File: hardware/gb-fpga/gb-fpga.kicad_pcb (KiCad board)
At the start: 2 copper layers, 1 part, among them U1 xc7s25ftgb196

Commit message: Basic boards setup
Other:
- copper layers 2 -> 4
- net class Default: via_dia 0.8 -> 0.5; via_drill 0.4 -> 0.3
- rule trace_min: 0.2 -> 0.15
- rule via_min_drill: 0.3 -> 0.2
- rule via_min_size: 0.4 -> 0.35
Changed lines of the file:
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@@
   (layers
     (0 F.Cu signal)
+    (1 In1.Cu power)
+    (2 In2.Cu power)
     (31 B.Cu signal)
     (32 B.Adhes user)
@@
     (zone_clearance 0.508)
     (zone_45_only no)
-    (trace_min 0.2)
-    (via_size 0.8)
-    (via_drill 0.4)
-    (via_min_size 0.4)
-    (via_min_drill 0.3)
+    (trace_min 0.15)
+    (via_size 0.5)
+    (via_drill 0.3)
+    (via_min_size 0.35)
+    (via_min_drill 0.2)
     (uvia_size 0.3)
     (uvia_drill 0.1)
@@
     (pcb_text_size 1.5 1.5)
     (mod_edge_width 0.12)
-    (mod_text_size 1 1)
+    (mod_text_size 1 0.8)
     (mod_text_width 0.15)
     (pad_size 1.524 1.524)
@@
     (clearance 0.2)
     (trace_width 0.25)
-    (via_dia 0.8)
-    (via_drill 0.4)
+    (via_dia 0.5)
+    (via_drill 0.3)
     (uvia_dia 0.3)
     (uvia_drill 0.1)

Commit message: Add GND net
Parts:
- added U2: MX25R3235FZNxx1, Package_SON:WSON-8-1EP_6x5mm_P1.27mm_EP3.4x4mm, F.Cu at (163.9, 30.7)
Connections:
- net Net-(U1-PadA1) renamed GND

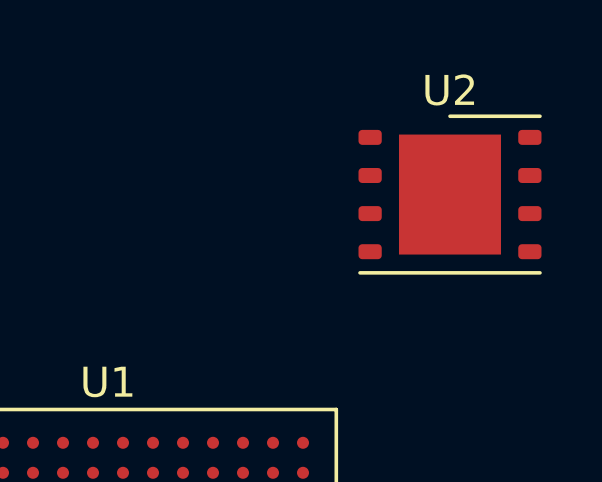
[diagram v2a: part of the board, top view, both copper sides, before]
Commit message: Use USON footprint for flash memory
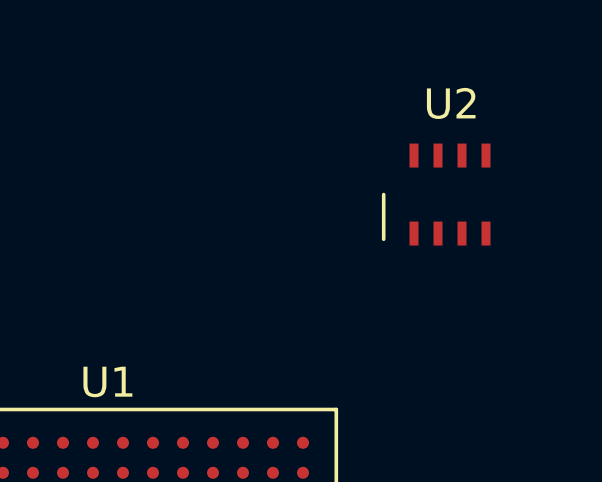
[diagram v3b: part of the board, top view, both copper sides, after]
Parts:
- U2: value MX25R3235FZNxx1 -> MX25R3235FZBxx1; footprint Package_SON:WSON-8-1EP_6x5mm_P1.27mm_EP3.4x4mm -> Package_SON:USON-8_4.0x3.0mm_P0.8mm
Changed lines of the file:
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@@
       (effects (font (size 1 1) (thickness 0.15)))
     )
+    (fp_line (start -7.61 7.61) (end -7.61 -6.61) (layer F.SilkS) (width 0.12))
+    (fp_line (start 7.61 7.61) (end -7.61 7.61) (layer F.SilkS) (width 0.12))
+    (fp_line (start 7.61 -7.61) (end 7.61 7.61) (layer F.SilkS) (width 0.12))
+    (fp_line (start -6.61 -7.61) (end 7.61 -7.61) (layer F.SilkS) (width 0.12))
+    (fp_line (start 8.5 -8.5) (end -8.5 -8.5) (layer F.CrtYd) (width 0.05))
+    (fp_line (start 8.5 8.5) (end 8.5 -8.5) (layer F.CrtYd) (width 0.05))
+    (fp_line (start -8.5 8.5) (end 8.5 8.5) (layer F.CrtYd) (width 0.05))
+    (fp_line (start -8.5 -8.5) (end -8.5 8.5) (layer F.CrtYd) (width 0.05))
+    (fp_line (start 7.5 -7.5) (end 7.5 7.5) (layer F.Fab) (width 0.1))
+    (fp_line (start -6.5 -7.5) (end 7.5 -7.5) (layer F.Fab) (width 0.1))
+    (fp_line (start -7.5 -6.5) (end -6.5 -7.5) (layer F.Fab) (width 0.1))
+    (fp_line (start -7.5 7.5) (end -7.5 -6.5) (layer F.Fab) (width 0.1))
     (fp_line (start 7.5 7.5) (end -7.5 7.5) (layer F.Fab) (width 0.1))
-    (fp_line (start -7.5 7.5) (end -7.5 -6.5) (layer F.Fab) (width 0.1))
-    (fp_line (start -7.5 -6.5) (end -6.5 -7.5) (layer F.Fab) (width 0.1))
-    (fp_line (start -6.5 -7.5) (end 7.5 -7.5) (layer F.Fab) (width 0.1))
-    (fp_line (start 7.5 -7.5) (end 7.5 7.5) (layer F.Fab) (width 0.1))
-    (fp_line (start -8.5 -8.5) (end -8.5 8.5) (layer F.CrtYd) (width 0.05))
-    (fp_line (start -8.5 8.5) (end 8.5 8.5) (layer F.CrtYd) (width 0.05))
-    (fp_line (start 8.5 8.5) (end 8.5 -8.5) (layer F.CrtYd) (width 0.05))
-    (fp_line (start 8.5 -8.5) (end -8.5 -8.5) (layer F.CrtYd) (width 0.05))
-    (fp_line (start -6.61 -7.61) (end 7.61 -7.61) (layer F.SilkS) (width 0.12))
-    (fp_line (start 7.61 -7.61) (end 7.61 7.61) (layer F.SilkS) (width 0.12))
-    (fp_line (start 7.61 7.61) (end -7.61 7.61) (layer F.SilkS) (width 0.12))
-    (fp_line (start -7.61 7.61) (end -7.61 -6.61) (layer F.SilkS) (width 0.12))
     (fp_text user %R (at 0 0) (layer F.Fab)
       (effects (font (size 1 1) (thickness 0.15)))
@@
     )
   )
-  (module Package_SON:WSON-8-1EP_6x5mm_P1.27mm_EP3.4x4mm (layer F.Cu)
+  (module Package_SON:USON-8_4.0x3.0mm_P0.8mm (layer F.Cu)
     (at 163.9 30.725)
-    (descr "WSON, 8 Pin (http://ww1.microchip.com/downloads/en/AppNotes/S72030.pdf), generated with kicad-footprint-generator ipc_noLead_generator.py")
-    (tags "WSON NoLead")
-    (attr smd)
-    (fp_text reference U2 (at 0 -3.45) (layer F.SilkS)
+    (fp_text reference U2 (at 0.05 -3) (layer F.SilkS)
       (effects (font (size 1 1) (thickness 0.15)))
     )
-    (fp_text value MX25R3235FZNxx1 (at 0 3.45) (layer F.Fab)
+    (fp_text value MX25R3235FZBxx1 (at -0.06 3.13) (layer F.Fab)
       (effects (font (size 1 1) (thickness 0.15)))
     )
-    (fp_line (start 3.3 -2.75) (end -3.3 -2.75) (layer F.CrtYd) (width 0.05))
-    (fp_line (start 3.3 2.75) (end 3.3 -2.75) (layer F.CrtYd) (width 0.05))
-    (fp_line (start -3.3 2.75) (end 3.3 2.75) (layer F.CrtYd) (width 0.05))
-    (fp_line (start -3.3 -2.75) (end -3.3 2.75) (layer F.CrtYd) (width 0.05))
-    (fp_line (start -3 -1.5) (end -2 -2.5) (layer F.Fab) (width 0.1))
-    (fp_line (start -3 2.5) (end -3 -1.5) (layer F.Fab) (width 0.1))
-    (fp_line (start 3 2.5) (end -3 2.5) (layer F.Fab) (width 0.1))
-    (fp_line (start 3 -2.5) (end 3 2.5) (layer F.Fab) (width 0.1))
-    (fp_line (start -2 -2.5) (end 3 -2.5) (layer F.Fab) (width 0.1))
-    (fp_line (start -3 2.61) (end 3 2.61) (layer F.SilkS) (width 0.12))
-    (fp_line (start 0 -2.61) (end 3 -2.61) (layer F.SilkS) (width 0.12))
-    (fp_text user %R (at 0 0) (layer F.Fab)
-      (effects (font (size 1 1) (thickness 0.15)))
-    )
-    (pad 1 smd roundrect (at -2.6625 -1.905) (size 0.775 0.5) (layers F.Cu F.Paste F.Mask) (roundrect_rratio 0.25)
+    (fp_line (start 2.39 1.98) (end 2.39 -1.99) (layer F.CrtYd) (width 0.12))
+    (fp_line (start -2.37 1.98) (end 2.39 1.98) (layer F.CrtYd) (width 0.12))
+    (fp_line (start -2.37 -1.99) (end -2.37 1.98) (layer F.CrtYd) (width 0.12))
+    (fp_line (start 2.39 -1.99) (end -2.37 -1.99) (layer F.CrtYd) (width 0.12))
+    (fp_line (start -2 -1.5) (end 2 -1.5) (layer F.Fab) (width 0.12))
+    (fp_line (start 2 -1.5) (end 2 1.5) (layer F.Fab) (width 0.12))
+    (fp_line (start 2 1.5) (end -2 1.5) (layer F.Fab) (width 0.12))
+    (fp_line (start -2 1.5) (end -2 -1.5) (layer F.Fab) (width 0.12))
+    (fp_line (start -2.21 1.49) (end -2.21 0) (layer F.SilkS) (width 0.12))
+    (pad 1 smd rect (at -1.2 1.3) (size 0.3 0.8) (layers F.Cu F.Paste F.Mask)
       (net 129 "Net-(U2-Pad1)"))
-    (pad 2 smd roundrect (at -2.6625 -0.635) (size 0.775 0.5) (layers F.Cu F.Paste F.Mask) (roundrect_rratio 0.25)
+    (pad 2 smd rect (at -0.4 1.3) (size 0.3 0.8) (layers F.Cu F.Paste F.Mask)
       (net 130 "Net-(U2-Pad2)"))
-    (pad 3 smd roundrect (at -2.6625 0.635) (size 0.775 0.5) (layers F.Cu F.Paste F.Mask) (roundrect_rratio 0.25)
+    (pad 3 smd rect (at 0.4 1.3) (size 0.3 0.8) (layers F.Cu F.Paste F.Mask)
       (net 131 "Net-(U2-Pad3)"))
-    (pad 4 smd roundrect (at -2.6625 1.905) (size 0.775 0.5) (layers F.Cu F.Paste F.Mask) (roundrect_rratio 0.25)
-      (net 128 GND))
-    (pad 5 smd roundrect (at 2.6625 1.905) (size 0.775 0.5) (layers F.Cu F.Paste F.Mask) (roundrect_rratio 0.25)
+    (pad 4 smd rect (at 1.2 1.3) (size 0.3 0.8) (layers F.Cu F.Paste F.Mask)
+      (net 128 GND))
+    (pad 5 smd rect (at 1.2 -1.3) (size 0.3 0.8) (layers F.Cu F.Paste F.Mask)
       (net 132 "Net-(U2-Pad5)"))
-    (pad 6 smd roundrect (at 2.6625 0.635) (size 0.775 0.5) (layers F.Cu F.Paste F.Mask) (roundrect_rratio 0.25)
+    (pad 6 smd rect (at 0.4 -1.3) (size 0.3 0.8) (layers F.Cu F.Paste F.Mask)
       (net 6 "Net-(U1-PadA8)"))
-    (pad 7 smd roundrect (at 2.6625 -0.635) (size 0.775 0.5) (layers F.Cu F.Paste F.Mask) (roundrect_rratio 0.25)
+    (pad 7 smd rect (at -0.4 -1.3) (size 0.3 0.8) (layers F.Cu F.Paste F.Mask)
       (net 133 "Net-(U2-Pad7)"))
-    (pad 8 smd roundrect (at 2.6625 -1.905) (size 0.775 0.5) (layers F.Cu F.Paste F.Mask) (roundrect_rratio 0.25)
+    (pad 8 smd rect (at -1.2 -1.3) (size 0.3 0.8) (layers F.Cu F.Paste F.Mask)
       (net 134 "Net-(U2-Pad8)"))
-    (pad 9 smd rect (at 0 0) (size 3.4 4) (layers F.Cu F.Mask)
-      (net 128 GND))
-    (pad "" smd roundrect (at -0.85 -1) (size 1.37 1.61) (layers F.Paste) (roundrect_rratio 0.182482))
-    (pad "" smd roundrect (at -0.85 1) (size 1.37 1.61) (layers F.Paste) (roundrect_rratio 0.182482))
-    (pad "" smd roundrect (at 0.85 -1) (size 1.37 1.61) (layers F.Paste) (roundrect_rratio 0.182482))
-    (pad "" smd roundrect (at 0.85 1) (size 1.37 1.61) (layers F.Paste) (roundrect_rratio 0.182482))
-    (model ${KISYS3DMOD}/Package_SON.3dshapes/WSON-8-1EP_6x5mm_P1.27mm_EP3.4x4mm.wrl
-      (at (xyz 0 0 0))
-      (scale (xyz 1 1 1))
-      (rotate (xyz 0 0 0))
-    )
   )
 )

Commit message: Use human readable names on pcb
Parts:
- U1: value xc7s25ftgb196 -> FPGA
- U2: value MX25R3235FZBxx1 -> Flash
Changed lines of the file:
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@@
       (effects (font (size 1 1) (thickness 0.15)))
     )
-    (fp_text value xc7s25ftgb196 (at 0 8.5) (layer F.Fab)
+    (fp_text value FPGA (at 0 8.5) (layer F.Fab)
       (effects (font (size 1 1) (thickness 0.15)))
     )
@@
       (effects (font (size 1 1) (thickness 0.15)))
     )
-    (fp_text value MX25R3235FZBxx1 (at -0.06 3.13) (layer F.Fab)
+    (fp_text value Flash (at -0.06 3.13) (layer F.Fab)
       (effects (font (size 1 1) (thickness 0.15)))
     )

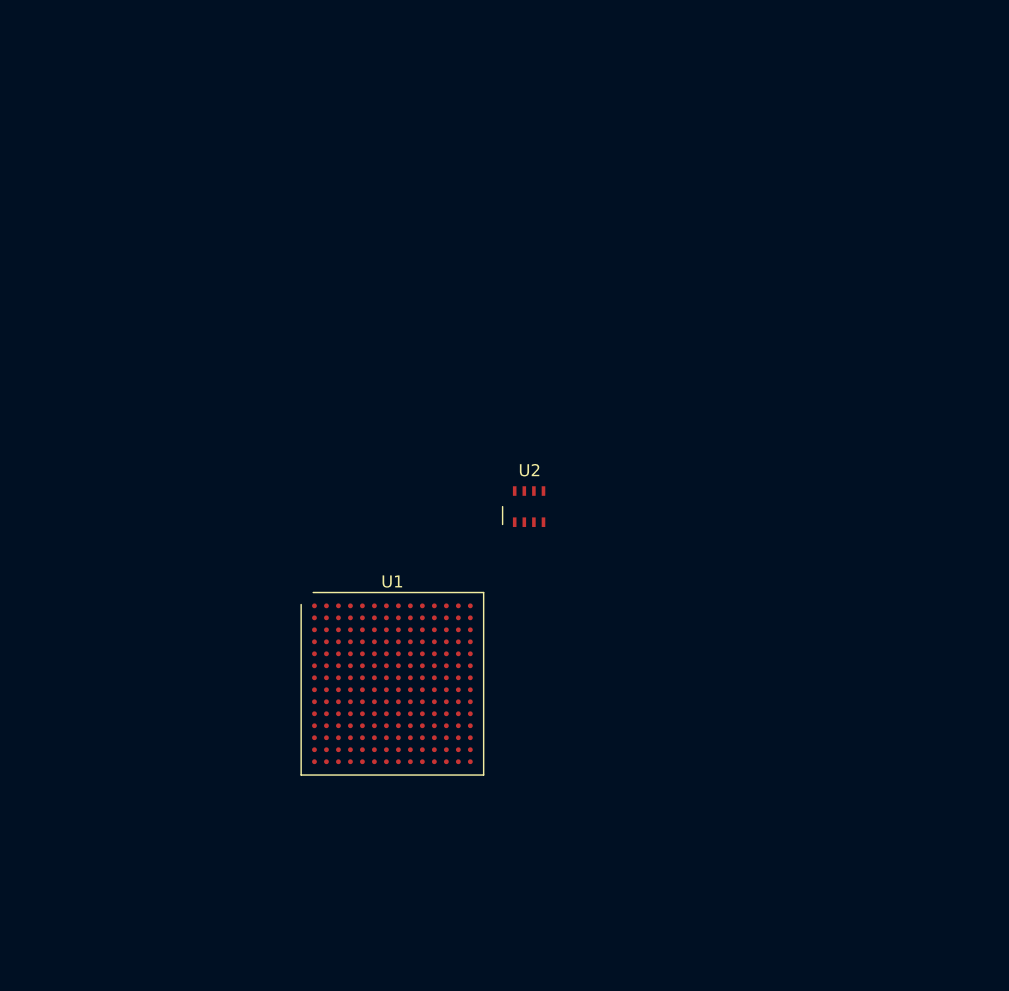
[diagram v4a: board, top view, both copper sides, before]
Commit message: Add board outline
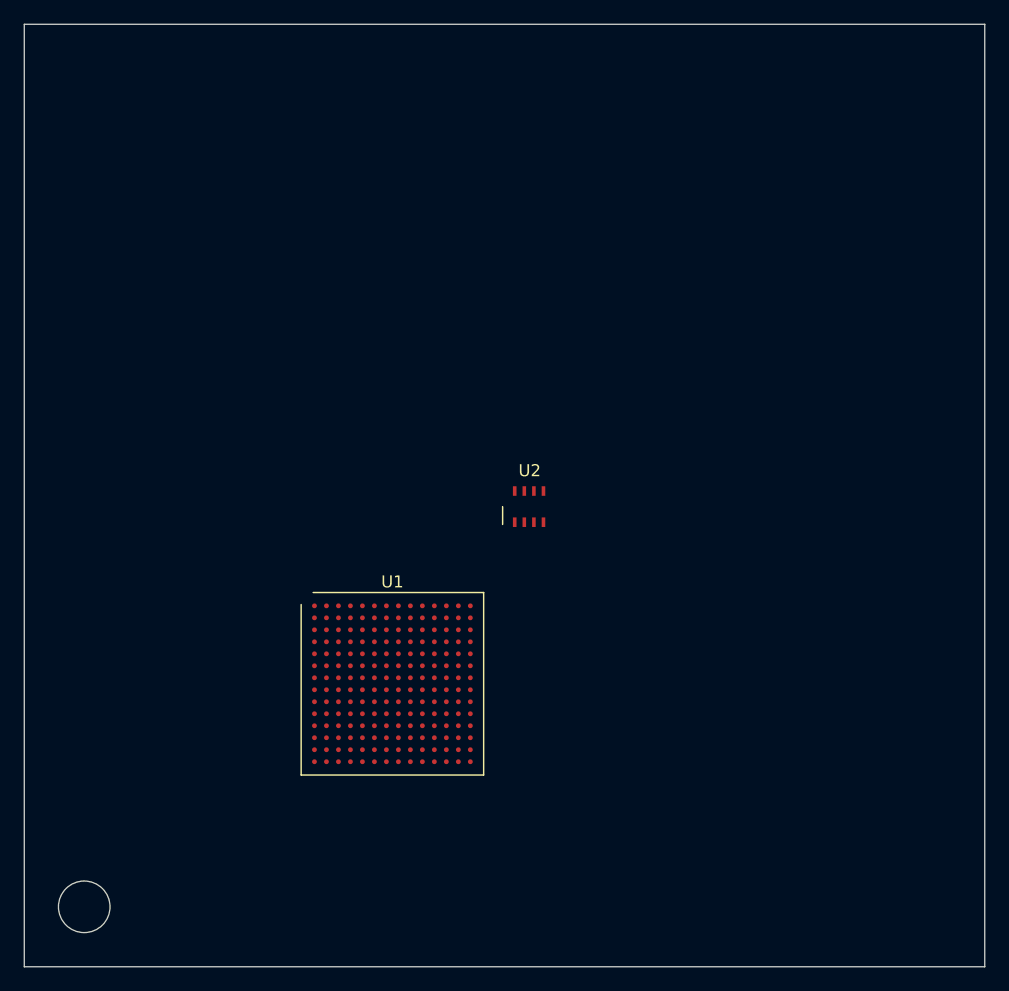
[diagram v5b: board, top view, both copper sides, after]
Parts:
- added REF**: MountingHole_4.3mm_M4_DIN965, MountingHole:MountingHole_4.3mm_M4_DIN965, F.Cu at (126.8, 64.1)
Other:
- board outline added: 80.1 x 78.6 mm
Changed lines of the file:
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@@
   (general
     (thickness 1.6)
-    (drawings 0)
+    (drawings 4)
     (tracks 0)
     (zones 0)
-    (modules 2)
+    (modules 3)
     (nets 135)
   )
@@
     (pad_drill 0.762)
     (pad_to_mask_clearance 0)
-    (aux_axis_origin 0 0)
+    (aux_axis_origin 121.8 69.1)
     (visible_elements FEFFFF7F)
     (pcbplotparams
@@
     (add_net "Net-(U2-Pad8)")
   )
+  (module MountingHole:MountingHole_4.3mm_M4_DIN965 (layer F.Cu)
+    (at 126.8 64.1)
+    (descr "Mounting Hole 4.3mm, no annular, M4, DIN965")
+    (tags "mounting hole 4.3mm no annular m4 din965")
+    (attr virtual)
+    (fp_text reference REF** (at 0 -4.75) (layer F.SilkS) hide
+      (effects (font (size 1 1) (thickness 0.15)))
+    )
+    (fp_text value MountingHole_4.3mm_M4_DIN965 (at 0 4.75) (layer F.Fab) hide
+      (effects (font (size 1 1) (thickness 0.15)))
+    )
+    (fp_text user %R (at 0.3 0) (layer F.Fab) hide
+      (effects (font (size 1 1) (thickness 0.15)))
+    )
+    (fp_circle (center 0 0) (end 3.75 0) (layer Cmts.User) (width 0.15))
+    (fp_circle (center 0 0) (end 4 0) (layer F.CrtYd) (width 0.05))
+    (pad 1 np_thru_hole circle (at 0 0) (size 4.3 4.3) (drill 4.3) (layers *.Cu *.Mask))
+  )
   (module Package_BGA:Xilinx_FTGB196 (layer F.Cu)
     (at 152.5 45.5)
@@
       (effects (font (size 1 1) (thickness 0.15)))
     )
+    (fp_line (start 7.5 7.5) (end -7.5 7.5) (layer F.Fab) (width 0.1))
+    (fp_line (start -7.5 7.5) (end -7.5 -6.5) (layer F.Fab) (width 0.1))
+    (fp_line (start -7.5 -6.5) (end -6.5 -7.5) (layer F.Fab) (width 0.1))
+    (fp_line (start -6.5 -7.5) (end 7.5 -7.5) (layer F.Fab) (width 0.1))
+    (fp_line (start 7.5 -7.5) (end 7.5 7.5) (layer F.Fab) (width 0.1))
+    (fp_line (start -8.5 -8.5) (end -8.5 8.5) (layer F.CrtYd) (width 0.05))
+    (fp_line (start -8.5 8.5) (end 8.5 8.5) (layer F.CrtYd) (width 0.05))
+    (fp_line (start 8.5 8.5) (end 8.5 -8.5) (layer F.CrtYd) (width 0.05))
+    (fp_line (start 8.5 -8.5) (end -8.5 -8.5) (layer F.CrtYd) (width 0.05))
+    (fp_line (start -6.61 -7.61) (end 7.61 -7.61) (layer F.SilkS) (width 0.12))
+    (fp_line (start 7.61 -7.61) (end 7.61 7.61) (layer F.SilkS) (width 0.12))
+    (fp_line (start 7.61 7.61) (end -7.61 7.61) (layer F.SilkS) (width 0.12))
     (fp_line (start -7.61 7.61) (end -7.61 -6.61) (layer F.SilkS) (width 0.12))
-    (fp_line (start 7.61 7.61) (end -7.61 7.61) (layer F.SilkS) (width 0.12))
-    (fp_line (start 7.61 -7.61) (end 7.61 7.61) (layer F.SilkS) (width 0.12))
-    (fp_line (start -6.61 -7.61) (end 7.61 -7.61) (layer F.SilkS) (width 0.12))
-    (fp_line (start 8.5 -8.5) (end -8.5 -8.5) (layer F.CrtYd) (width 0.05))
-    (fp_line (start 8.5 8.5) (end 8.5 -8.5) (layer F.CrtYd) (width 0.05))
-    (fp_line (start -8.5 8.5) (end 8.5 8.5) (layer F.CrtYd) (width 0.05))
-    (fp_line (start -8.5 -8.5) (end -8.5 8.5) (layer F.CrtYd) (width 0.05))
-    (fp_line (start 7.5 -7.5) (end 7.5 7.5) (layer F.Fab) (width 0.1))
-    (fp_line (start -6.5 -7.5) (end 7.5 -7.5) (layer F.Fab) (width 0.1))
-    (fp_line (start -7.5 -6.5) (end -6.5 -7.5) (layer F.Fab) (width 0.1))
-    (fp_line (start -7.5 7.5) (end -7.5 -6.5) (layer F.Fab) (width 0.1))
-    (fp_line (start 7.5 7.5) (end -7.5 7.5) (layer F.Fab) (width 0.1))
     (fp_text user %R (at 0 0) (layer F.Fab)
       (effects (font (size 1 1) (thickness 0.15)))
@@
       (effects (font (size 1 1) (thickness 0.15)))
     )
+    (fp_line (start -2.21 1.49) (end -2.21 0) (layer F.SilkS) (width 0.12))
+    (fp_line (start -2 1.5) (end -2 -1.5) (layer F.Fab) (width 0.12))
+    (fp_line (start 2 1.5) (end -2 1.5) (layer F.Fab) (width 0.12))
+    (fp_line (start 2 -1.5) (end 2 1.5) (layer F.Fab) (width 0.12))
+    (fp_line (start -2 -1.5) (end 2 -1.5) (layer F.Fab) (width 0.12))
+    (fp_line (start 2.39 -1.99) (end -2.37 -1.99) (layer F.CrtYd) (width 0.12))
+    (fp_line (start -2.37 -1.99) (end -2.37 1.98) (layer F.CrtYd) (width 0.12))
+    (fp_line (start -2.37 1.98) (end 2.39 1.98) (layer F.CrtYd) (width 0.12))
     (fp_line (start 2.39 1.98) (end 2.39 -1.99) (layer F.CrtYd) (width 0.12))
-    (fp_line (start -2.37 1.98) (end 2.39 1.98) (layer F.CrtYd) (width 0.12))
-    (fp_line (start -2.37 -1.99) (end -2.37 1.98) (layer F.CrtYd) (width 0.12))
-    (fp_line (start 2.39 -1.99) (end -2.37 -1.99) (layer F.CrtYd) (width 0.12))
-    (fp_line (start -2 -1.5) (end 2 -1.5) (layer F.Fab) (width 0.12))
-    (fp_line (start 2 -1.5) (end 2 1.5) (layer F.Fab) (width 0.12))
-    (fp_line (start 2 1.5) (end -2 1.5) (layer F.Fab) (width 0.12))
-    (fp_line (start -2 1.5) (end -2 -1.5) (layer F.Fab) (width 0.12))
-    (fp_line (start -2.21 1.49) (end -2.21 0) (layer F.SilkS) (width 0.12))
     (pad 1 smd rect (at -1.2 1.3) (size 0.3 0.8) (layers F.Cu F.Paste F.Mask)
       (net 129 "Net-(U2-Pad1)"))
@@
       (net 134 "Net-(U2-Pad8)"))
   )
+  (gr_line (start 121.8 -9.5) (end 121.8 69.1) (layer Edge.Cuts) (width 0.05))
+  (gr_line (start 201.9 -9.5) (end 121.8 -9.5) (layer Edge.Cuts) (width 0.05))
+  (gr_line (start 201.9 69.1) (end 201.9 -9.5) (layer Edge.Cuts) (width 0.05))
+  (gr_line (start 121.8 69.1) (end 201.9 69.1) (layer Edge.Cuts) (width 0.05))
 )
